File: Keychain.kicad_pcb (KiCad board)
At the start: 4 copper layers, 106.7 x 78.7 mm, 60 parts, among them U1 IMX6UL_BGA289, U2 DDR3_BGA96

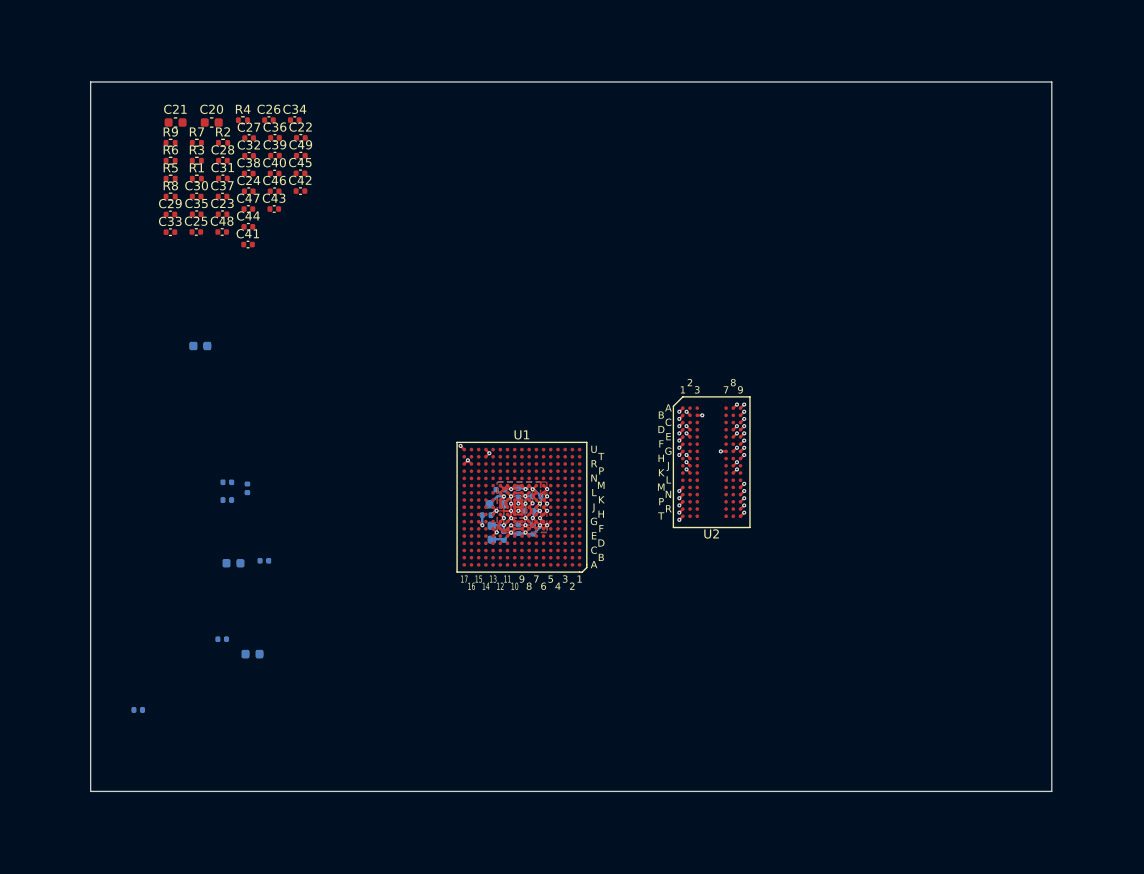
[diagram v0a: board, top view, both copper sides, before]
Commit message: DDR nets are connected, now needs length tuning
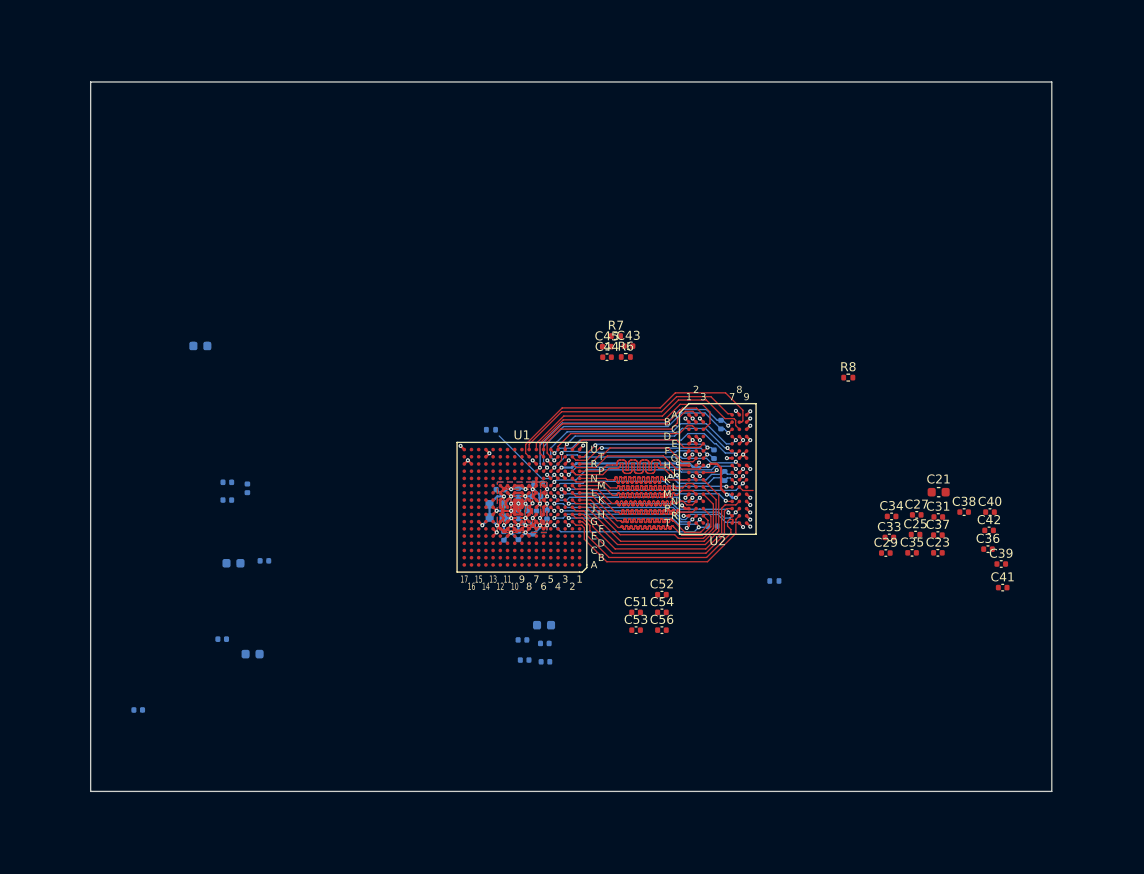
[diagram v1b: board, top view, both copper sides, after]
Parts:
- removed C48, C49: 2.2pF, Capacitor_SMD:C_0402_1005Metric
- removed R2: 10K, Resistor_SMD:R_0402_1005Metric
- removed R9: 240, Resistor_SMD:R_0402_1005Metric
- added C51: 0.22uF, Capacitor_SMD:C_0402_1005Metric, F.Cu at (159.6, 97.0)
- added C52: 0.22uF, Capacitor_SMD:C_0402_1005Metric, F.Cu at (162.5, 95.0)
- added C53: 0.22uF, Capacitor_SMD:C_0402_1005Metric, F.Cu at (159.6, 98.9)
- added C54: 0.22uF, Capacitor_SMD:C_0402_1005Metric, F.Cu at (162.5, 97.0)
- added C56: 0.22uF, Capacitor_SMD:C_0402_1005Metric, F.Cu at (162.5, 98.9)
- C20, C22, C24, C26, C28, C30, C32, C46, C47, R1, R3, R4, R5: moved to B.Cu
- moved C21 94.1 mm to (193.2, 83.6)
- moved C39 92.5 mm to (200.1, 91.6)
- moved C41 92.0 mm to (200.3, 94.2)
- moved C36 91.4 mm to (198.7, 90.0)
- moved C23 87.8 mm to (193.1, 90.4)
- moved C29 87.8 mm to (187.3, 90.4)
- moved C31 87.8 mm to (193.1, 86.4)
- moved C35 87.8 mm to (190.2, 90.4)
- moved C37 87.8 mm to (193.1, 88.4)
- moved C38 87.8 mm to (196.0, 85.8)
- moved C40 87.8 mm to (198.9, 85.8)
- moved C33 86.7 mm to (187.7, 88.7)
- moved C25 86.6 mm to (190.6, 88.3)
- moved C42 85.2 mm to (198.8, 87.9)
- moved C27 85.1 mm to (190.8, 86.2)
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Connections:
- C20 pad 1: DRAM_1V35 -> +1V5
- C21 pad 1: DRAM_1V35 -> Net-(C21-Pad1)
- C22 pad 1: DRAM_1V35 -> +1V5
- C23 pad 1: DRAM_1V35 -> Net-(C21-Pad1)
- C24 pad 1: DRAM_1V35 -> +1V5
- C25 pad 1: DRAM_1V35 -> Net-(C21-Pad1)
- C26 pad 1: DRAM_1V35 -> +1V5
- C27 pad 1: DRAM_1V35 -> Net-(C21-Pad1)
- C28 pad 1: DRAM_1V35 -> +1V5
- C29 pad 1: DRAM_1V35 -> Net-(C21-Pad1)
- C30 pad 1: DRAM_1V35 -> +1V5
- C31 pad 1: DRAM_1V35 -> Net-(C21-Pad1)
- C32 pad 1: DRAM_1V35 -> +1V5
- C33 pad 1: DRAM_1V35 -> Net-(C21-Pad1)
- C35 pad 1: DRAM_1V35 -> Net-(C21-Pad1)
- C37 pad 1: DRAM_1V35 -> Net-(C21-Pad1)
- C38 pad 1: DRAM_1V35 -> Net-(C21-Pad1)
- C40 pad 1: DRAM_1V35 -> Net-(C21-Pad1)
- C42 pad 1: DRAM_1V35 -> Net-(C21-Pad1)
- C43 pad 1: DRAM_1V35 -> +1V5
- C44 pad 1: DRAM_1V35 -> +1V5
- C46 pad 1: /DDR/DQSL+ -> /DDR/DQSU+
- C46 pad 2: /DDR/DQSL- -> /DDR/DQSU-
- C47 pad 1: /DDR/DQSU+ -> /DDR/DQSL+
- C47 pad 2: /DDR/DQSU- -> /DDR/DQSL-
- R6 pad 2: DRAM_1V35 -> +1V5
- U1 pad F1: /DDR/ODT1 -> Net-(U1-PadF1)
- U1 pad G6: DRAM_1V35 -> +1V5
- U1 pad H5: /DDR/CS1# -> Net-(U1-PadH5)
- U1 pad H6: DRAM_1V35 -> +1V5
- U1 pad J3: /DDR/CKE1 -> Net-(U1-PadJ3)
- U1 pad J6: DRAM_1V35 -> +1V5
- U1 pad K5: /DDR/A15 -> Net-(U1-PadK5)
- U1 pad K6: DRAM_1V35 -> +1V5
- U1 pad L6: DRAM_1V35 -> +1V5
- U1 pad M6: DRAM_1V35 -> +1V5
- U2 pad A1: DRAM_1V35 -> +1V5
- U2 pad A2: /DDR/DQU5 -> /DDR/DQL6
- U2 pad A3: /DDR/DQU7 -> /DDR/DQL1
- U2 pad A7: /DDR/DQU4 -> /DDR/DQL4
- U2 pad A8: DRAM_1V35 -> +1V5
- U2 pad B2: DRAM_1V35 -> +1V5
- U2 pad B7: /DDR/DQSU- -> /DDR/DQSL-
- U2 pad B8: /DDR/DQU6 -> /DDR/DQL5
- U2 pad C1: DRAM_1V35 -> +1V5
- U2 pad C2: /DDR/DQU3 -> /DDR/DQL7
- U2 pad C3: /DDR/DQU1 -> /DDR/DQL2
- U2 pad C7: /DDR/DQSU+ -> /DDR/DQSL+
- U2 pad C8: /DDR/DQU2 -> /DDR/DQL3
- U2 pad C9: DRAM_1V35 -> +1V5
- U2 pad D2: DRAM_1V35 -> +1V5
- U2 pad D7: /DDR/DQU0 -> /DDR/DQL0
- U2 pad D9: DRAM_1V35 -> +1V5
- U2 pad E3: /DDR/DQL0 -> /DDR/DQU0
- U2 pad E9: DRAM_1V35 -> +1V5
- U2 pad F1: DRAM_1V35 -> +1V5
- U2 pad F2: /DDR/DQL7 -> /DDR/DQU3
- U2 pad F3: /DDR/DQSL+ -> /DDR/DQSU+
- U2 pad F7: /DDR/DQL4 -> /DDR/DQU1
- U2 pad F8: /DDR/DQL3 -> /DDR/DQU2
- U2 pad G2: /DDR/DQL6 -> /DDR/DQU7
- U2 pad G3: /DDR/DQSL- -> /DDR/DQSU-
- U2 pad G7: DRAM_1V35 -> +1V5
- U2 pad H2: DRAM_1V35 -> +1V5
- U2 pad H3: /DDR/DQL1 -> /DDR/DQU6
- U2 pad H7: /DDR/DQL2 -> /DDR/DQU5
- U2 pad H8: /DDR/DQL5 -> /DDR/DQU4
- U2 pad H9: DRAM_1V35 -> +1V5
- U2 pad J1: /DDR/ODT1 -> Net-(U2-PadJ1)
- U2 pad J9: /DDR/CKE1 -> Net-(U2-PadJ9)
- U2 pad K2: DRAM_1V35 -> +1V5
- U2 pad K8: DRAM_1V35 -> +1V5
- U2 pad L1: /DDR/CS1# -> Net-(U2-PadL1)
- U2 pad L9: /DDR/ZQ1 -> Net-(U2-PadL9)
- U2 pad M7: /DDR/A15 -> Net-(U2-PadM7)
- U2 pad N1: DRAM_1V35 -> +1V5
- U2 pad N9: DRAM_1V35 -> +1V5
- U2 pad R1: DRAM_1V35 -> +1V5
- U2 pad R9: DRAM_1V35 -> +1V5
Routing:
- net /DDR/DQL5: track 0.00 -> 30.4 mm
- net /DDR/CK-: track 0.00 -> 27.9 mm, vias 0 -> 2
- net /DDR/DQSL-: track 0.00 -> 26.9 mm, vias 0 -> 2
- net /DDR/DQL3: track 0.00 -> 26.9 mm
- net /DDR/DQSL+: track 0.00 -> 26.6 mm, vias 0 -> 2
- net /DDR/CK+: track 0.00 -> 26.3 mm, vias 0 -> 2
- net /DDR/DQL4: track 0.00 -> 26.2 mm
- net /DDR/DQL0: track 0.00 -> 25.4 mm, vias 0 -> 2
- net VREFDDR: track 0.00 -> 25.2 mm, vias 0 -> 5
- net /DDR/A9: track 0.00 -> 25.1 mm
- net /DDR/CAS#: track 0.00 -> 25.0 mm
- net /DDR/DQL2: track 0.00 -> 25.0 mm
- net /DDR/A3: track 0.00 -> 24.7 mm
- net /DDR/ODT0: track 0.00 -> 24.5 mm
- net /DDR/A2: track 0.00 -> 24.3 mm
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- added copper zone on B.Cu, net +1V5

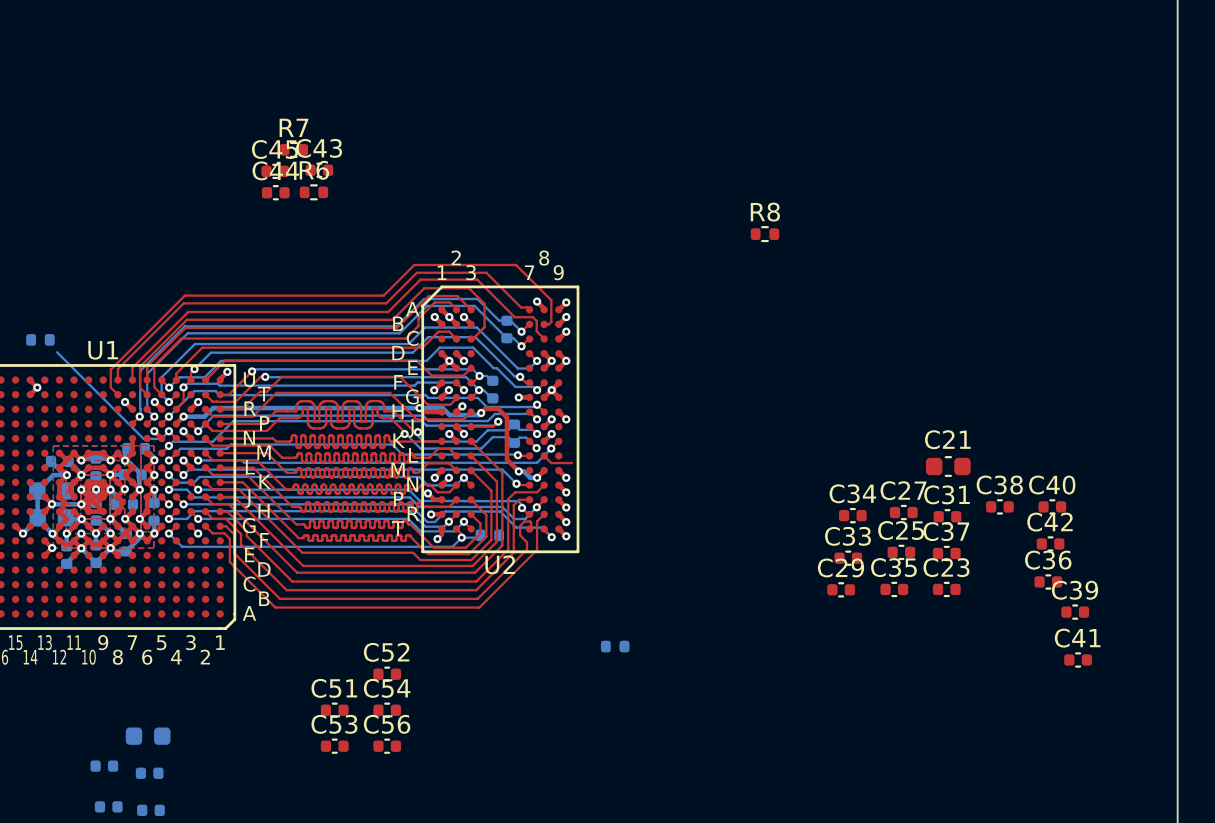
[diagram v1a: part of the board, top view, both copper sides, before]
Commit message: Completed DDR routing & length matching
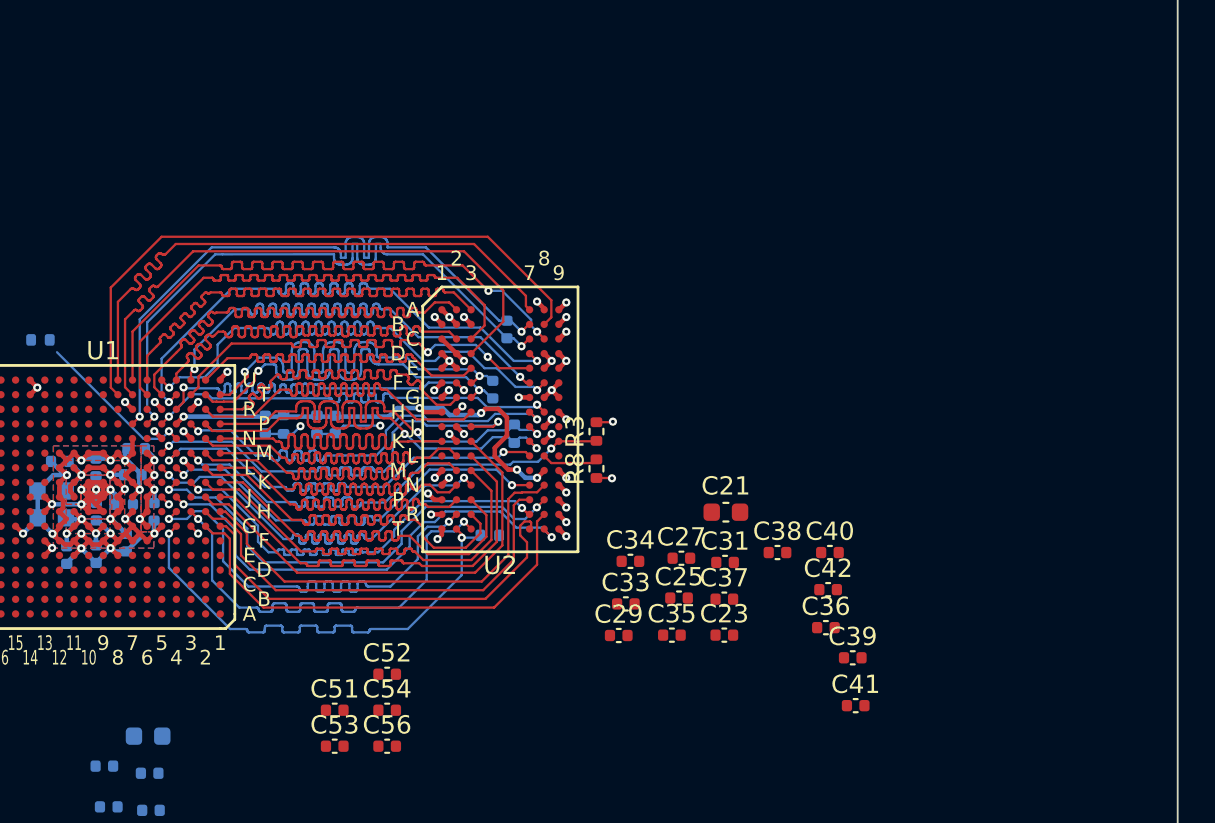
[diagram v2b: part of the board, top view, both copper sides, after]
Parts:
- removed C43: 4.7uF, Capacitor_SMD:C_0402_1005Metric
- C44, C45, R6, R7: moved to B.Cu
- R3: moved to F.Cu
- moved R8 15.8 mm to (173.9, 83.8), turned to 90 degrees
- moved R7 15.0 mm to (156.8, 81.3), turned to 90 degrees
- moved C45 13.9 mm to (155.8, 81.3), turned to 270 degrees
- moved C44 13.1 mm to (159.6, 81.3), turned to 90 degrees
- moved R6 12.7 mm to (158.6, 81.3), turned to 270 degrees
- moved C21 12.4 mm to (181.0, 86.1)
- moved C25 12.4 mm to (178.4, 90.8)
- moved C27 12.4 mm to (178.6, 88.7)
- moved C33 12.4 mm to (175.5, 91.2)
- moved C34 12.4 mm to (175.8, 88.8)
- moved C42 12.4 mm to (186.6, 90.4)
- moved C23 12.4 mm to (180.9, 92.9)
- moved C29 12.4 mm to (175.1, 92.9)
- moved C31 12.4 mm to (181.0, 88.9)
- moved C35 12.4 mm to (178.1, 92.9)
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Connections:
- U2 pad D3: /DDR/DMU -> /DDR/DML
- U2 pad E7: /DDR/DML -> /DDR/DMU
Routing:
- net /DDR/DML: track 0.00 -> 33.0 mm
- net /DDR/DMU: track 0.01 -> 25.1 mm, vias 0 -> 2
- net /DDR/DQL7: track 16.8 -> 31.8 mm
- net /DDR/DQL6: track 20.2 -> 33.5 mm
- net /DDR/DQL1: track 20.4 -> 32.9 mm
- net /DDR/DQU1: track 20.8 -> 31.9 mm
- net /DDR/DQU2: track 23.2 -> 33.6 mm
- net /DDR/DQU7: track 14.5 -> 23.7 mm
- net /DDR/DQSU+: track 16.4 -> 25.5 mm
- net /DDR/DQU6: track 16.0 -> 25.0 mm
- net /DDR/DQSU-: track 17.6 -> 26.5 mm
- net /DDR/A13: track 16.2 -> 25.0 mm
- net /DDR/DQL2: track 25.0 -> 33.1 mm
- net /DDR/DQSL-: track 26.9 -> 34.9 mm
- net /DDR/RESET#: track 18.8 -> 26.7 mm
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- added copper zone on PWR, net +1V5

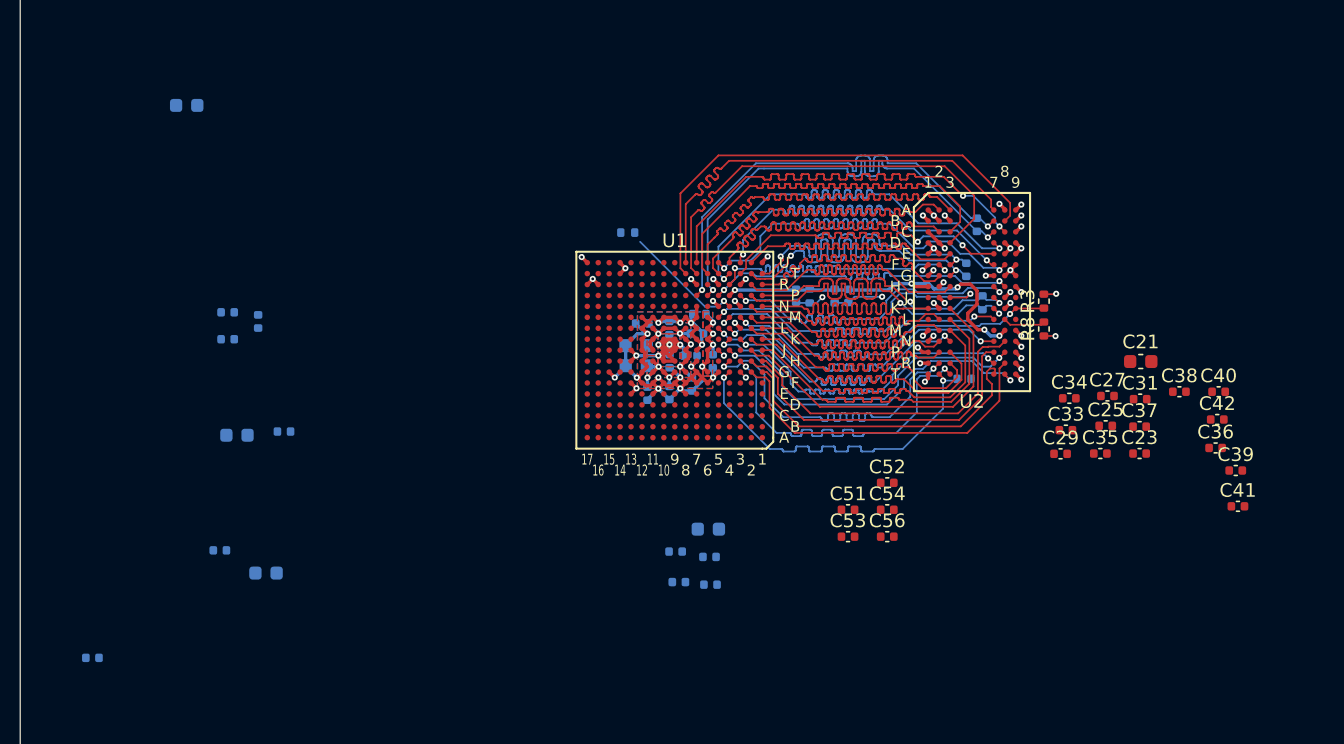
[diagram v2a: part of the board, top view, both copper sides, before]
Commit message: Added some LDO and connectors, still need to finish routing
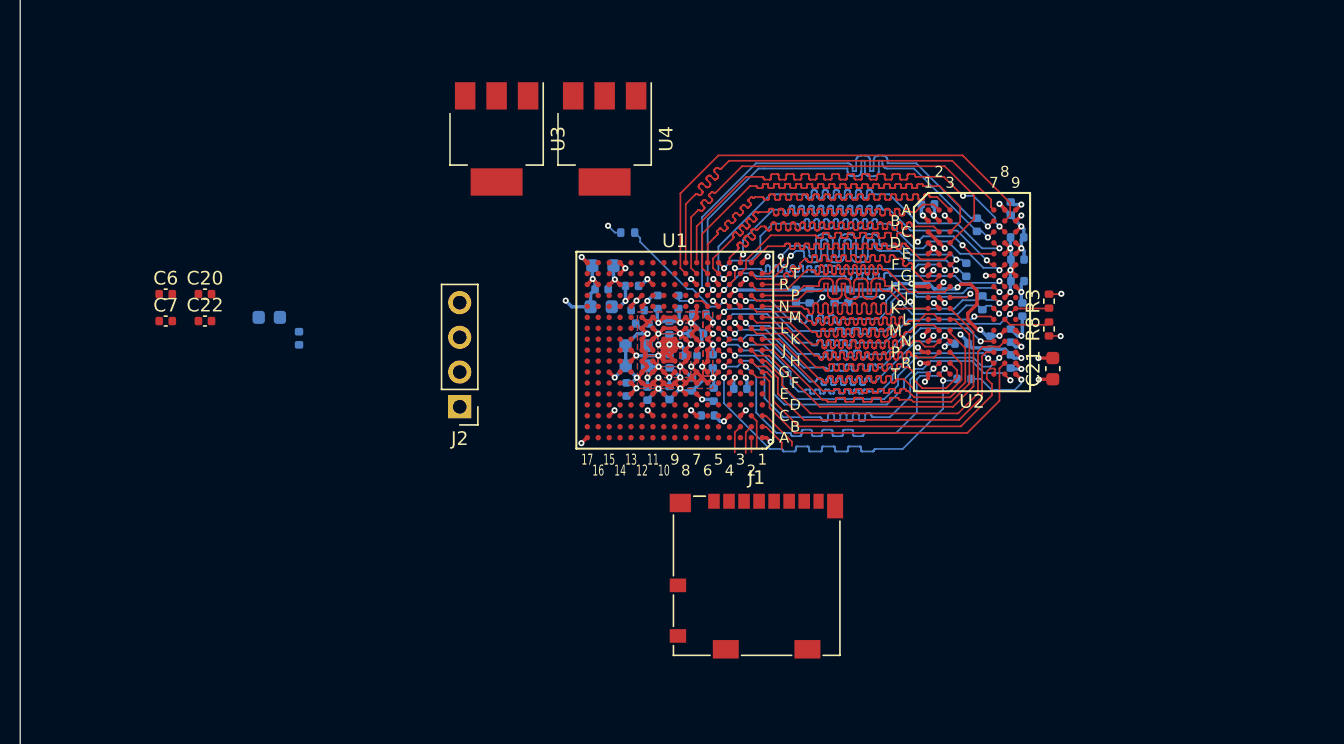
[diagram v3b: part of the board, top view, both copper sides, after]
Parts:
- removed C30, C32, C34, C40, C41, C42, C56: 0.22uF, Capacitor_SMD:C_0402_1005Metric
- added J1: Micro_SD_Card, Connector_Card:microSD_HC_Molex_104031-0811, F.Cu at (152.9, 101.8)
- added J2: Conn_01x04, Connector_PinHeader_2.54mm:PinHeader_1x04_P2.54mm_Vertical, F.Cu at (131.2, 89.4)
- added U3: AZ1117C-3.3, Package_TO_SOT_SMD:SOT-223, F.Cu at (133.9, 69.8)
- added U4: AZ1117C-1.5, Package_TO_SOT_SMD:SOT-223, F.Cu at (141.8, 69.8)
- C20: footprint Capacitor_SMD:C_0603_1608Metric -> Capacitor_SMD:C_0402_1005Metric; moved to F.Cu
- C22, C7: value 0.22uF -> 22uF; moved to F.Cu
- C23, C25, C27, C29, C31, C33, C35, C36, C37, C38, C39, C51, C52, C53, C54: moved to B.Cu
- C24: value 0.22uF -> 10uF
- C6: value 0.22uF -> 10uF; moved to F.Cu
- moved C11 48.8 mm to (145.7, 81.8), turned to 270 degrees
- moved C22 40.7 mm to (112.6, 83.2)
- moved C36 40.7 mm to (147.2, 81.8), turned to 270 degrees
- moved C20 40.6 mm to (112.6, 81.2)
- moved C26 35.1 mm to (119.5, 84.4), turned to 270 degrees
- moved C17 33.8 mm to (141.6, 80.8), turned to 180 degrees
- moved C19 33.4 mm to (141.7, 79.1), turned to 180 degrees
- moved C4 30.0 mm to (144.2, 82.4)
- moved C14 28.2 mm to (141.6, 82.1), turned to 180 degrees
- moved C10 27.6 mm to (143.8, 80.6)
- moved C37 22.5 mm to (165.4, 74.6), turned to 180 degrees
- moved C39 20.2 mm to (170.0, 84.8), turned to 270 degrees
- moved C53 19.5 mm to (143.4, 88.2), turned to 90 degrees
- moved C23 18.2 mm to (172.0, 77.0), turned to 180 degrees
- moved C33 16.7 mm to (171.5, 74.9), turned to 90 degrees
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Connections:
- C20 pad 1: +1V5 -> +5V
- C21 pad 1: Net-(C21-Pad1) -> +1V5
- C23 pad 1: Net-(C21-Pad1) -> +1V5
- C25 pad 1: Net-(C21-Pad1) -> +1V5
- C27 pad 1: Net-(C21-Pad1) -> +1V5
- C29 pad 1: Net-(C21-Pad1) -> +1V5
- C31 pad 1: Net-(C21-Pad1) -> +1V5
- C33 pad 1: Net-(C21-Pad1) -> +1V5
- C35 pad 1: Net-(C21-Pad1) -> +1V5
- C37 pad 1: Net-(C21-Pad1) -> +1V5
- C38 pad 1: Net-(C21-Pad1) -> +1V5
- C6 pad 1: +1V5 -> +5V
- C7 pad 1: +1V5 -> +3V3
- U1 pad A2: Net-(U1-PadA2) -> SD_D3
- U1 pad B1: Net-(U1-PadB1) -> SD_D2
- U1 pad B2: Net-(U1-PadB2) -> SD_D1
- U1 pad B3: Net-(U1-PadB3) -> SD_D0
- U1 pad C1: Net-(U1-PadC1) -> SD_CLK
- U1 pad C2: Net-(U1-PadC2) -> SD_CMD
- U1 pad J14: Net-(U1-PadJ14) -> Debug_RTS
- U1 pad K14: Net-(U1-PadK14) -> Debug_TX
- U1 pad K15: Net-(U1-PadK15) -> Debug_CTS
- U1 pad K16: Net-(U1-PadK16) -> Debug_RX
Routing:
- net GND: track 74.4 -> 111.4 mm, vias 44 -> 55
- net +1V5: track 21.7 -> 34.9 mm, vias 20 -> 23
- net +3V3: track 20.4 -> 25.7 mm, vias 6 -> 9
- net SD_CLK: track 0.00 -> 3.26 mm
- net HIGH_CAP: track 0.00 -> 3.08 mm, vias 0 -> 1
- net NVCC_PLL: track 0.00 -> 2.85 mm, vias 0 -> 1
- net VDD_HIGH_CAP: track 0.00 -> 2.64 mm, vias 0 -> 1
- net SD_CMD: track 0.00 -> 2.48 mm
- net SD_D2: track 0.00 -> 2.40 mm
- net SD_D1: track 0.00 -> 2.09 mm
- net SD_D0: track 0.00 -> 2.05 mm
- net SNVS_CAP: track 0.00 -> 1.48 mm, vias 0 -> 1
- net SD_D3: track 0.00 -> 1.07 mm
- net /DDR/ZQPAD: track 8.83 -> 9.67 mm
- added copper zone on PWR, net +3V3
